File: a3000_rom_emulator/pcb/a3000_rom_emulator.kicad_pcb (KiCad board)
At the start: 4 copper layers, 99.1 x 88.9 mm, 37 parts

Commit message: In-progress A3000 ROM emulator board
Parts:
- removed the REF** at (142.2, 66.0)
- removed the REF** at (142.2, 45.7)
- removed the REF** at (142.2, 86.4)
- removed the REF** at (142.2, 106.7)
- added ROM1: ROM header, Package_DIP:DIP-32_W15.24mm, F.Cu at (142.2, 45.7)
- added ROM2: ROM header, myelin-kicad:dip32_rom_data_only, F.Cu at (170.2, 58.4)
- added ROM3: ROM header, myelin-kicad:dip32_rom_data_only, F.Cu at (170.2, 78.7)
- added ROM4: ROM header, myelin-kicad:dip32_rom_data_only, F.Cu at (170.2, 99.1)
- moved REF** 84.5 mm to (175.2, 38.4)
- moved CPLD 39.4 mm to (155.3, 55.0)
- moved FC0 39.4 mm to (159.8, 70.2)
- moved FC3 39.4 mm to (159.8, 82.3)
- moved FLASH2 39.4 mm to (153.7, 70.2)
- moved FLASH3 39.4 mm to (153.7, 82.2)
- moved FC1 39.4 mm to (147.4, 70.8)
- moved FC2 39.4 mm to (156.3, 72.3)
- moved FC4 39.4 mm to (147.3, 82.6)
- moved FC5 39.4 mm to (156.4, 84.3)
- moved staple_single4 28.2 mm to (239.4, 33.0)
- moved staple_single7 27.2 mm to (238.1, 29.2)

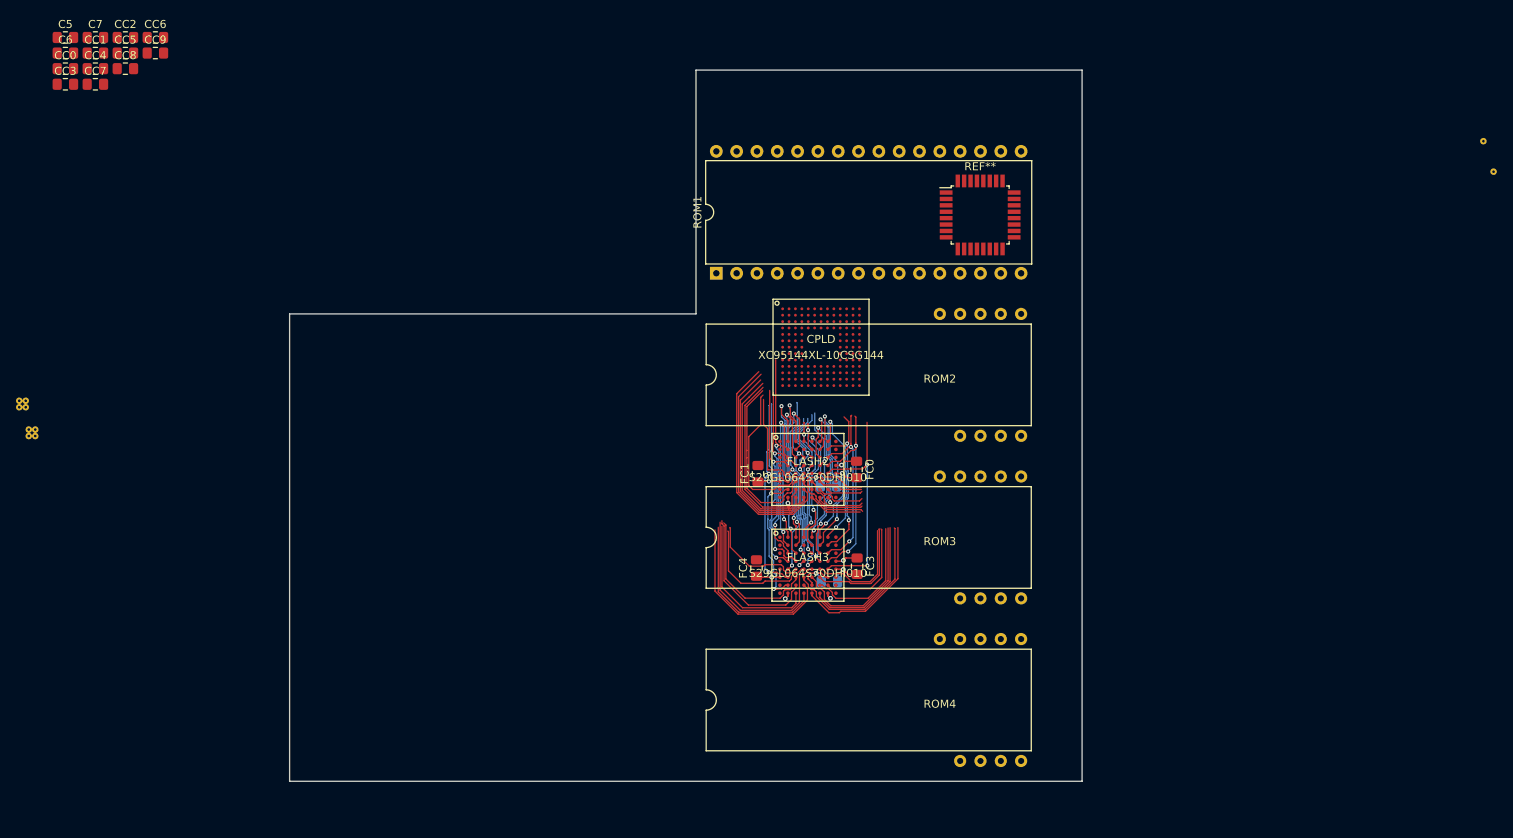
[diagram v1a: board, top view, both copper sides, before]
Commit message: Fixed hole sizes in sockets, and removed flash2-5
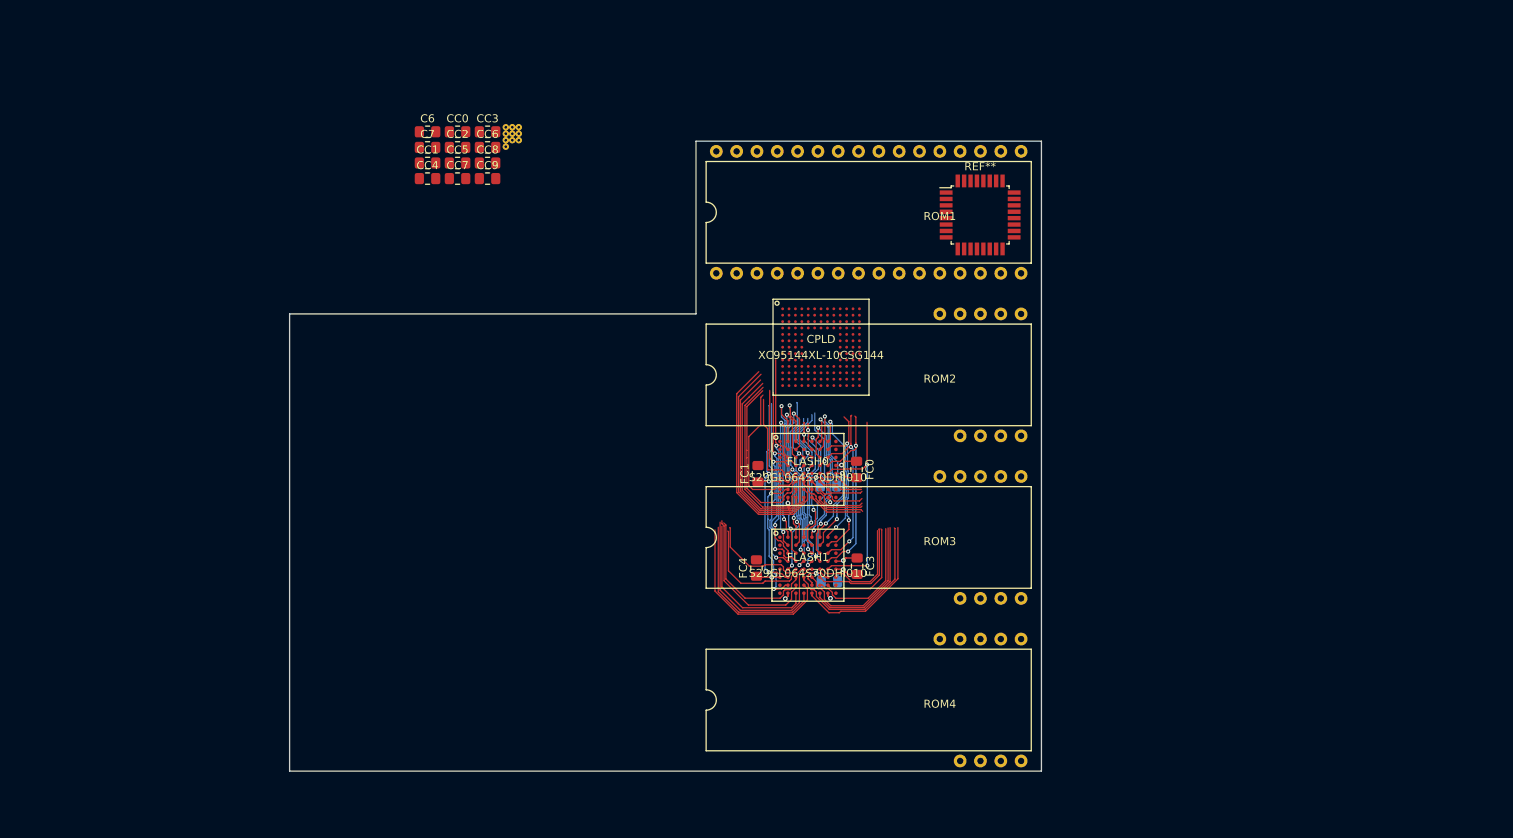
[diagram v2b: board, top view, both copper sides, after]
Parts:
- removed C5: 100n, Capacitor_SMD:C_0805_2012Metric_Pad1.15x1.40mm_HandSolder
- ROM1: footprint Package_DIP:DIP-32_W15.24mm -> myelin-kicad:dip32_rom
- moved staple_single7 122.2 mm to (115.9, 29.9)
- moved staple_single4 122.0 mm to (117.5, 27.5)
- moved staple_single3 71.7 mm to (116.7, 27.5)
- moved staple_single9 71.2 mm to (117.5, 28.3)
- moved staple_single5 70.6 mm to (116.7, 28.3)
- moved staple_single1 70.6 mm to (115.9, 27.5)
- moved staple_single10 70.1 mm to (117.5, 29.1)
- moved staple_single2 69.5 mm to (115.9, 28.3)
- moved staple_single6 69.0 mm to (115.9, 29.1)
- moved staple_single8 69.0 mm to (116.7, 29.1)
- moved CC3 53.1 mm to (113.6, 28.0)
- moved CC0 49.7 mm to (109.9, 28.0)
- moved CC7 46.8 mm to (109.9, 33.9)
- moved CC8 46.8 mm to (113.6, 31.9)
- moved C6 46.3 mm to (106.1, 28.0)
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- renumbered FLASH2 to FLASH0, FLASH3 to FLASH1
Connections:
- net D0 renamed rom_D0
- net D1 renamed rom_D1
- net D10 renamed rom_D10
- net D11 renamed rom_D11
- net D12 renamed rom_D12
- net D13 renamed rom_D13
- net D14 renamed rom_D14
- net D15 renamed rom_D15
- net D16 renamed rom_D16
- net D17 renamed rom_D17
- net D18 renamed rom_D18
- net D19 renamed rom_D19
- net D2 renamed rom_D2
- net D20 renamed rom_D20
- net D21 renamed rom_D21
- net D22 renamed rom_D22
- net D23 renamed rom_D23
- net D24 renamed rom_D24
- net D25 renamed rom_D25
- net D26 renamed rom_D26
- net D27 renamed rom_D27
- net D28 renamed rom_D28
- net D29 renamed rom_D29
- net D3 renamed rom_D3
- net D30 renamed rom_D30
- net D31 renamed rom_D31
- net D4 renamed rom_D4
- net D5 renamed rom_D5
- net D6 renamed rom_D6
- net D7 renamed rom_D7
- net D8 renamed rom_D8
- net D9 renamed rom_D9
- net flash2_DQ0 renamed flash0_DQ0
- net flash2_DQ1 renamed flash0_DQ1
- net flash2_DQ10 renamed flash0_DQ10
- net flash2_DQ11 renamed flash0_DQ11
- net flash2_DQ12 renamed flash0_DQ12
- net flash2_DQ13 renamed flash0_DQ13
- net flash2_DQ14 renamed flash0_DQ14
- net flash2_DQ15 renamed flash0_DQ15
- net flash2_DQ2 renamed flash0_DQ2
- net flash2_DQ3 renamed flash0_DQ3
- net flash2_DQ4 renamed flash0_DQ4
- net flash2_DQ5 renamed flash0_DQ5
- net flash2_DQ6 renamed flash0_DQ6
- net flash2_DQ7 renamed flash0_DQ7
- net flash2_DQ8 renamed flash0_DQ8
- net flash2_DQ9 renamed flash0_DQ9
- net flash3_DQ0 renamed flash1_DQ0
- net flash3_DQ1 renamed flash1_DQ1
- net flash3_DQ10 renamed flash1_DQ10
- net flash3_DQ11 renamed flash1_DQ11
- net flash3_DQ12 renamed flash1_DQ12
- net flash3_DQ13 renamed flash1_DQ13
- net flash3_DQ14 renamed flash1_DQ14
- net flash3_DQ15 renamed flash1_DQ15
- net flash3_DQ2 renamed flash1_DQ2
- net flash3_DQ3 renamed flash1_DQ3
- net flash3_DQ4 renamed flash1_DQ4
- net flash3_DQ5 renamed flash1_DQ5
- net flash3_DQ6 renamed flash1_DQ6
- net flash3_DQ7 renamed flash1_DQ7
- net flash3_DQ8 renamed flash1_DQ8
- net flash3_DQ9 renamed flash1_DQ9
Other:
- board size 99.1 x 88.9 mm -> 94 x 78.7 mm
- board text added: "On the A3000, we have a small gap to the right of the roms, and the keyboard connector to the left of ROM 1. About 0.2" above ROM 1 but zero clearance below ROM 4. On A310, there's a tantalum cap and podule backplane connector to the right of the roms, but about 0.3" clearance below them before we hit a protruding jumper. Board edge is about 0.1" above ROM 1."

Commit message: a3000_rom_emulator: all components placed, ready to route the big CPLD I think
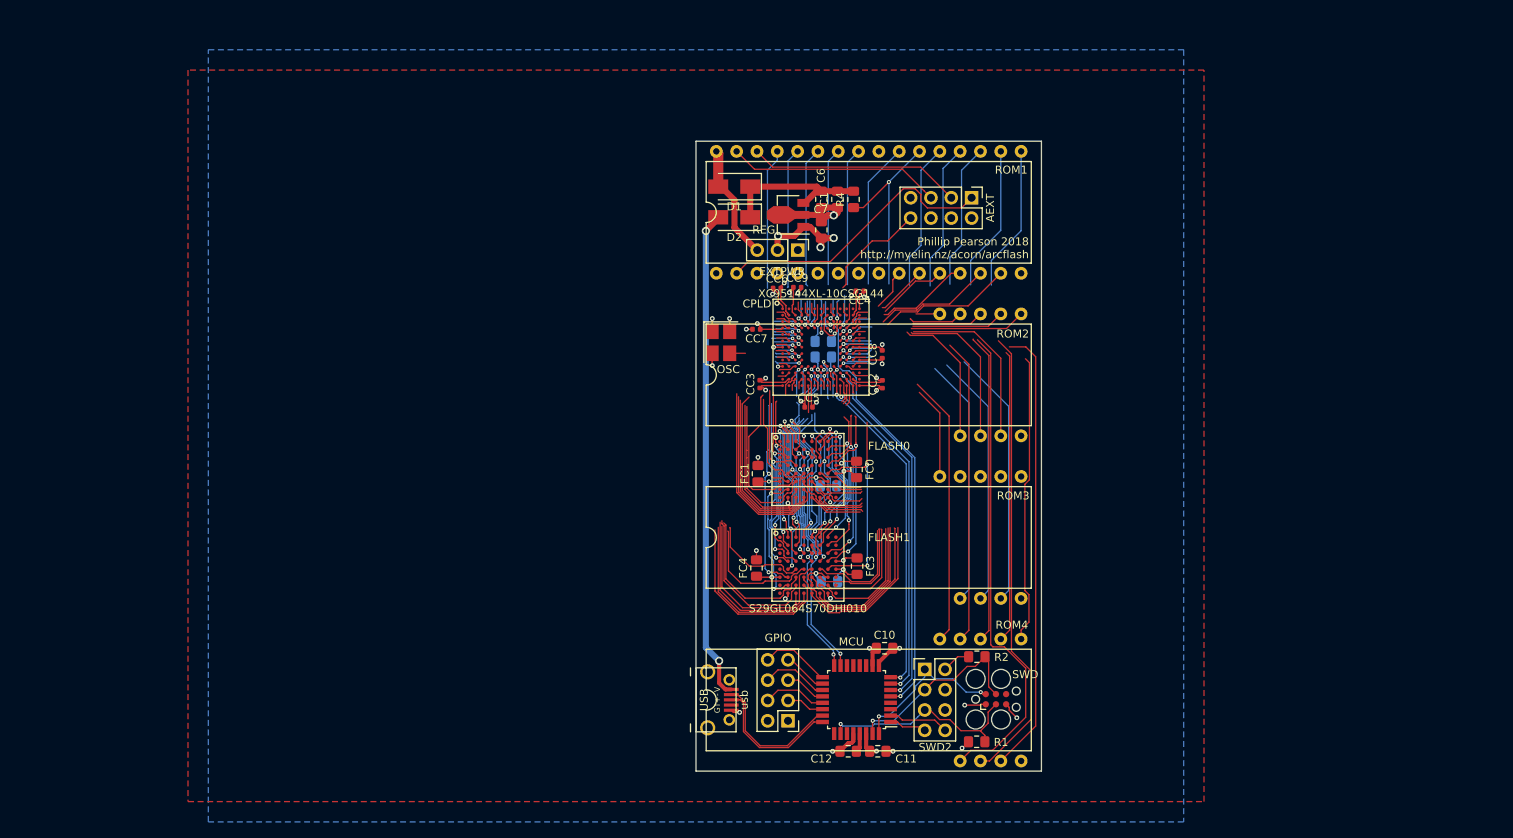
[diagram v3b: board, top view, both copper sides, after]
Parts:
- removed REF**: TQFP-32_7x7mm_P0.8mm, Package_QFP:TQFP-32_7x7mm_P0.8mm
- removed staple_single1, staple_single10, staple_single2, staple_single3, staple_single4, staple_single5, staple_single6, staple_single7, staple_single8, staple_single9: , myelin-kicad:via_single
- added AEXT: Extras, Connector_PinHeader_2.54mm:PinHeader_2x04_P2.54mm_Vertical, F.Cu at (174.2, 36.3)
- added C1: 10u, Capacitor_SMD:C_0805_2012Metric_Pad1.15x1.40mm_HandSolder, F.Cu at (157.4, 36.5)
- added C10: 100n, Capacitor_SMD:C_0805_2012Metric_Pad1.15x1.40mm_HandSolder, F.Cu at (163.3, 92.6)
- added C11: 100n, Capacitor_SMD:C_0805_2012Metric_Pad1.15x1.40mm_HandSolder, F.Cu at (162.4, 105.5)
- added C12: 1u, Capacitor_SMD:C_0805_2012Metric_Pad1.15x1.40mm_HandSolder, F.Cu at (158.7, 105.5)
- added D1: S1ATR, Diode_SMD:D_SMA, F.Cu at (144.5, 34.9)
- added D2: S1ATR, Diode_SMD:D_SMA, F.Cu at (144.5, 38.7)
- added EXTPWR: ext pwr, Connector_PinHeader_2.54mm:PinHeader_1x03_P2.54mm_Vertical, F.Cu at (152.4, 42.8)
- added GPIO: gpio, Connector_PinHeader_2.54mm:PinHeader_2x04_P2.54mm_Vertical, F.Cu at (151.2, 101.7)
- added MCU: ATSAMD21E18A, Package_QFP:TQFP-32_7x7mm_P0.8mm, F.Cu at (159.8, 99.0)
- added OSC: osc, Oscillator:Oscillator_SMD_Abracon_ASE-4Pin_3.2x2.5mm_HandSoldering, F.Cu at (142.8, 54.3)
- added R1: 10k, Resistor_SMD:R_0805_2012Metric_Pad1.15x1.40mm_HandSolder, F.Cu at (174.8, 104.3)
- added R2: 1k, Resistor_SMD:R_0805_2012Metric_Pad1.15x1.40mm_HandSolder, F.Cu at (174.8, 93.7)
- added R4: 10k, Resistor_SMD:R_0805_2012Metric_Pad1.15x1.40mm_HandSolder, F.Cu at (159.4, 36.5)
- added REG: AP7365-33YG-XX, Package_TO_SOT_SMD:SOT-89-3, F.Cu at (151.6, 38.4)
- added SWD: swd, Tag-Connect_TC2030-IDC-FP_2x03_P1.27mm_Vertical, F.Cu at (177.2, 99.0)
- added SWD2: swd, Connector_PinHeader_2.54mm:PinHeader_2x04_P2.54mm_Vertical, F.Cu at (168.3, 95.2)
- added USB: usb, myelin-kicad:micro_usb_b_smd_molex, F.Cu at (141.7, 99.0)
- CC0, CC1: moved to B.Cu
- CC2, CC3, CC4, CC5, CC6, CC7, CC8, CC9: footprint Capacitor_SMD:C_0805_2012Metric_Pad1.15x1.40mm_HandSolder -> Capacitor_SMD:C_0402_1005Metric
- moved CC2 60.8 mm to (163.0, 59.6), turned to 90 degrees
- moved CC4 55.8 mm to (160.2, 47.9), turned to 180 degrees
- moved CC8 54.8 mm to (163.0, 55.8), turned to 90 degrees
- moved CC1 54.3 mm to (155.6, 54.2)
- moved CC0 53.7 mm to (155.6, 56.2)
- moved CC5 53.5 mm to (153.8, 62.5)
- moved C7 50.3 mm to (155.4, 40.3), turned to 90 degrees
- moved C6 49.9 mm to (155.4, 36.5), turned to 90 degrees
- moved CC3 46.4 mm to (147.7, 59.6), turned to 90 degrees
- moved CC7 41.8 mm to (147.2, 52.7), turned to 180 degrees
- moved CC9 41.0 mm to (152.4, 47.5)
- moved CC6 40.2 mm to (149.8, 47.6)
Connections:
- CPLD pad A1: (no net) -> 3V3
- CPLD pad A10: (no net) -> dummy_A10
- CPLD pad A11: (no net) -> dummy_A11
- CPLD pad A12: (no net) -> dummy_A12
- CPLD pad A13: (no net) -> 3V3
- CPLD pad A2: (no net) -> arc_RESET
- CPLD pad A3: (no net) -> dummy_A3
- CPLD pad A4: (no net) -> dummy_A4
- CPLD pad A5: (no net) -> dummy_A5
- CPLD pad A6: (no net) -> dummy_A6
- CPLD pad A7: (no net) -> dummy_A7
- CPLD pad A8: (no net) -> dummy_A8
- CPLD pad A9: (no net) -> dummy_A9
- CPLD pad B1: (no net) -> dummy_B1
- CPLD pad B10: (no net) -> dummy_B10
- CPLD pad B11: (no net) -> dummy_B11
- CPLD pad B12: (no net) -> GND
- CPLD pad B13: (no net) -> dummy_B13
- CPLD pad B2: (no net) -> GND
- CPLD pad B3: (no net) -> 3V3
- CPLD pad B4: (no net) -> dummy_B4
- CPLD pad B5: (no net) -> dummy_B5
- CPLD pad B6: (no net) -> dummy_B6
- CPLD pad B7: (no net) -> dummy_B7
- CPLD pad B8: (no net) -> GND
- CPLD pad B9: (no net) -> dummy_B9
- CPLD pad C1: (no net) -> dummy_C1
- CPLD pad C10: (no net) -> GND
- CPLD pad C11: (no net) -> dummy_C11
- CPLD pad C12: (no net) -> dummy_C12
- CPLD pad C13: (no net) -> dummy_C13
- CPLD pad C2: (no net) -> dummy_C2
- CPLD pad C3: (no net) -> dummy_C3
- CPLD pad C4: (no net) -> dummy_C4
- CPLD pad C5: (no net) -> dummy_C5
- CPLD pad C6: (no net) -> dummy_C6
- CPLD pad C7: (no net) -> 3V3
- CPLD pad C8: (no net) -> cpld_TDO
- CPLD pad C9: (no net) -> dummy_C9
- CPLD pad D1: (no net) -> 3V3
- CPLD pad D10: (no net) -> dummy_D10
- CPLD pad D11: (no net) -> dummy_D11
- CPLD pad D12: (no net) -> dummy_D12
- CPLD pad D13: (no net) -> dummy_D13
- CPLD pad D2: (no net) -> dummy_D2
- CPLD pad D3: (no net) -> dummy_D3
- CPLD pad D4: (no net) -> dummy_D4
- CPLD pad D5: (no net) -> dummy_D5
- CPLD pad D6: (no net) -> dummy_D6
- CPLD pad D7: (no net) -> dummy_D7
- CPLD pad D8: (no net) -> dummy_D8
- CPLD pad D9: (no net) -> dummy_D9
- CPLD pad E1: (no net) -> dummy_E1
- CPLD pad E10: (no net) -> dummy_E10
- CPLD pad E11: (no net) -> GND
- CPLD pad E12: (no net) -> dummy_E12
- CPLD pad E13: (no net) -> dummy_E13
- CPLD pad E2: (no net) -> dummy_E2
- CPLD pad E3: (no net) -> dummy_E3
- CPLD pad E4: (no net) -> dummy_E4
- CPLD pad F1: (no net) -> dummy_F1
- CPLD pad F10: (no net) -> dummy_F10
- CPLD pad F11: (no net) -> dummy_F11
- CPLD pad F12: (no net) -> dummy_F12
- CPLD pad F13: (no net) -> dummy_F13
- CPLD pad F2: (no net) -> dummy_F2
- CPLD pad F3: (no net) -> dummy_F3
- CPLD pad F4: (no net) -> dummy_F4
- CPLD pad G1: (no net) -> GND
- CPLD pad G10: (no net) -> dummy_G10
- CPLD pad G11: (no net) -> dummy_G11
- CPLD pad G12: (no net) -> GND
- CPLD pad G13: (no net) -> GND
- CPLD pad G2: (no net) -> dummy_G2
- CPLD pad G3: (no net) -> dummy_G3
- CPLD pad G4: (no net) -> dummy_G4
- CPLD pad H1: (no net) -> dummy_H1
- CPLD pad H10: (no net) -> dummy_H10
- CPLD pad H11: (no net) -> dummy_H11
- CPLD pad H12: (no net) -> dummy_H12
- CPLD pad H13: (no net) -> dummy_H13
- CPLD pad H2: (no net) -> dummy_H2
- CPLD pad H3: (no net) -> dummy_H3
- CPLD pad H4: (no net) -> dummy_H4
- CPLD pad J1: (no net) -> dummy_J1
- CPLD pad J10: (no net) -> dummy_J10
- CPLD pad J11: (no net) -> dummy_J11
- CPLD pad J12: (no net) -> dummy_J12
- CPLD pad J13: (no net) -> 3V3
- CPLD pad J2: (no net) -> dummy_J2
- CPLD pad J3: (no net) -> dummy_J3
- CPLD pad J4: (no net) -> dummy_J4
- CPLD pad K1: (no net) -> GND
- CPLD pad K10: (no net) -> dummy_K10
- CPLD pad K11: (no net) -> dummy_K11
- CPLD pad K12: (no net) -> dummy_K12
- CPLD pad K13: (no net) -> dummy_K13
- CPLD pad K2: (no net) -> dummy_K2_GCK1
- CPLD pad K3: (no net) -> dummy_K3
- CPLD pad K4: (no net) -> dummy_K4
- CPLD pad K5: (no net) -> dummy_K5
- CPLD pad K6: (no net) -> dummy_K6
- CPLD pad K7: (no net) -> dummy_K7
- CPLD pad K8: (no net) -> dummy_K8
- CPLD pad K9: (no net) -> dummy_K9
- CPLD pad L1: (no net) -> dummy_L1_GCK2
- CPLD pad L10: (no net) -> cpld_TCK
- CPLD pad L11: (no net) -> dummy_L11
- CPLD pad L12: (no net) -> dummy_L12
- CPLD pad L13: (no net) -> dummy_L13
- CPLD pad L2: (no net) -> dummy_L2
- CPLD pad L3: (no net) -> dummy_L3
- CPLD pad L4: (no net) -> 3V3
- CPLD pad L5: (no net) -> dummy_L5
- CPLD pad L6: (no net) -> dummy_L6
- CPLD pad L7: (no net) -> 3V3
- CPLD pad L8: (no net) -> dummy_L8
- CPLD pad L9: (no net) -> cpld_TDI
- CPLD pad M1: (no net) -> dummy_M1
- CPLD pad M10: (no net) -> dummy_M10
- CPLD pad M11: (no net) -> dummy_M11
- CPLD pad M12: (no net) -> GND
- CPLD pad M13: (no net) -> dummy_M13
- CPLD pad M2: (no net) -> GND
- CPLD pad M3: (no net) -> dummy_M3
- CPLD pad M4: (no net) -> dummy_M4
- CPLD pad M5: (no net) -> GND
- CPLD pad M6: (no net) -> dummy_M6
- CPLD pad M7: (no net) -> dummy_M7
- CPLD pad M8: (no net) -> dummy_M8
- CPLD pad M9: (no net) -> GND
- CPLD pad N1: (no net) -> 3V3
- CPLD pad N10: (no net) -> cpld_TMS
- CPLD pad N11: (no net) -> dummy_N11
- CPLD pad N12: (no net) -> dummy_N12
- CPLD pad N13: (no net) -> 3V3
- CPLD pad N2: (no net) -> dummy_N2_GCK3
- CPLD pad N3: (no net) -> dummy_N3
- CPLD pad N4: (no net) -> dummy_N4
- CPLD pad N5: (no net) -> dummy_N5
- CPLD pad N6: (no net) -> dummy_N6
- CPLD pad N7: (no net) -> dummy_N7
- CPLD pad N8: (no net) -> dummy_N8
- CPLD pad N9: (no net) -> dummy_N9
- ROM1 pad 2: rom_A16 -> rom_A16_ext
- ROM1 pad 30: rom_A17 -> rom_A17_ext
- ROM1 pad 31: rom_A18 -> rom_A18_ext
- ROM1 pad 32: 5V -> rom_5V
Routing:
- net GND: track 10.8 -> 80.0 mm, vias 6 -> 28
- net 3V3: track 21.8 -> 87.7 mm, vias 6 -> 25
- net VUSB: track 0.00 -> 61.4 mm, vias 0 -> 2
- net rom_D24: track 0.00 -> 61.0 mm
- net rom_D25: track 0.00 -> 57.5 mm
- net rom_D26: track 0.00 -> 56.1 mm
- net cpld_TDO: track 0.00 -> 54.0 mm, vias 0 -> 2
- net cpld_TCK: track 0.00 -> 45.2 mm, vias 0 -> 2
- net cpld_TDI: track 0.00 -> 43.6 mm, vias 0 -> 2
- net cpld_TMS: track 0.00 -> 42.7 mm, vias 0 -> 2
- net rom_D29: track 0.00 -> 38.7 mm
- net rom_D30: track 0.00 -> 38.2 mm
- net rom_D28: track 0.00 -> 36.4 mm
- net rom_D27: track 0.00 -> 36.1 mm
- net rom_A16_ext: track 0.00 -> 35.8 mm
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- added copper zone on B.Cu, net GND
- added copper zone on F.Cu, net GND
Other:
- board size 94 x 78.7 mm -> 43.2 x 78.7 mm
- board text added: "Phillip Pearson 2018 http://myelin.nz/acorn/arcflash"
- board text added: "http://myelin.nz/acorn/arcflash by Phillip Pearson, pp@myelin.nz Copyright 2018 Google LLC"
- board text added: "myelin.nz"
